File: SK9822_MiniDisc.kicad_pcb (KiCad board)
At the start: 4 copper layers, 220 x 220 mm, 341 parts, among them P1 CONN_01X04, P2 CONN_01X04

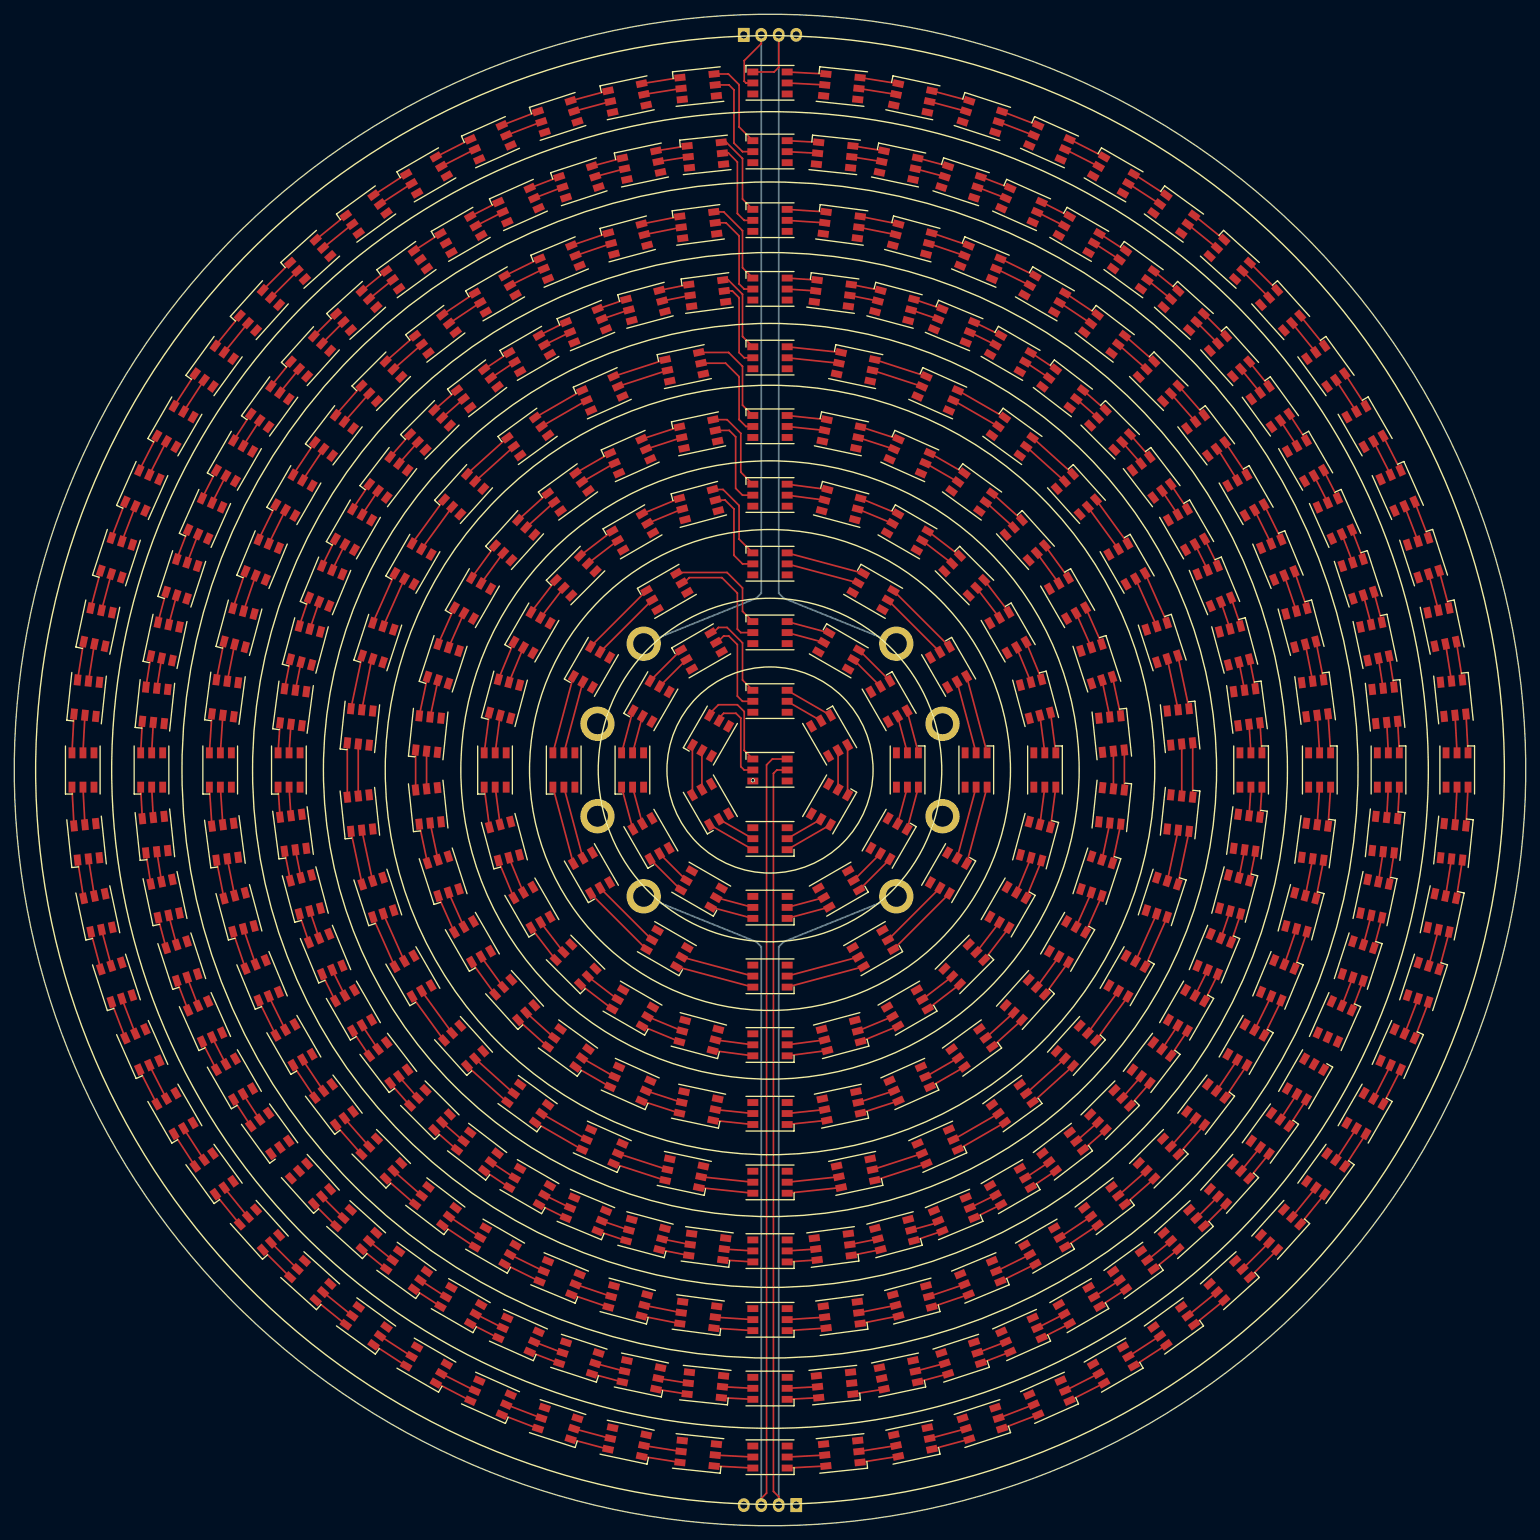
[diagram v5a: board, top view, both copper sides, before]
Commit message: Grounds laid
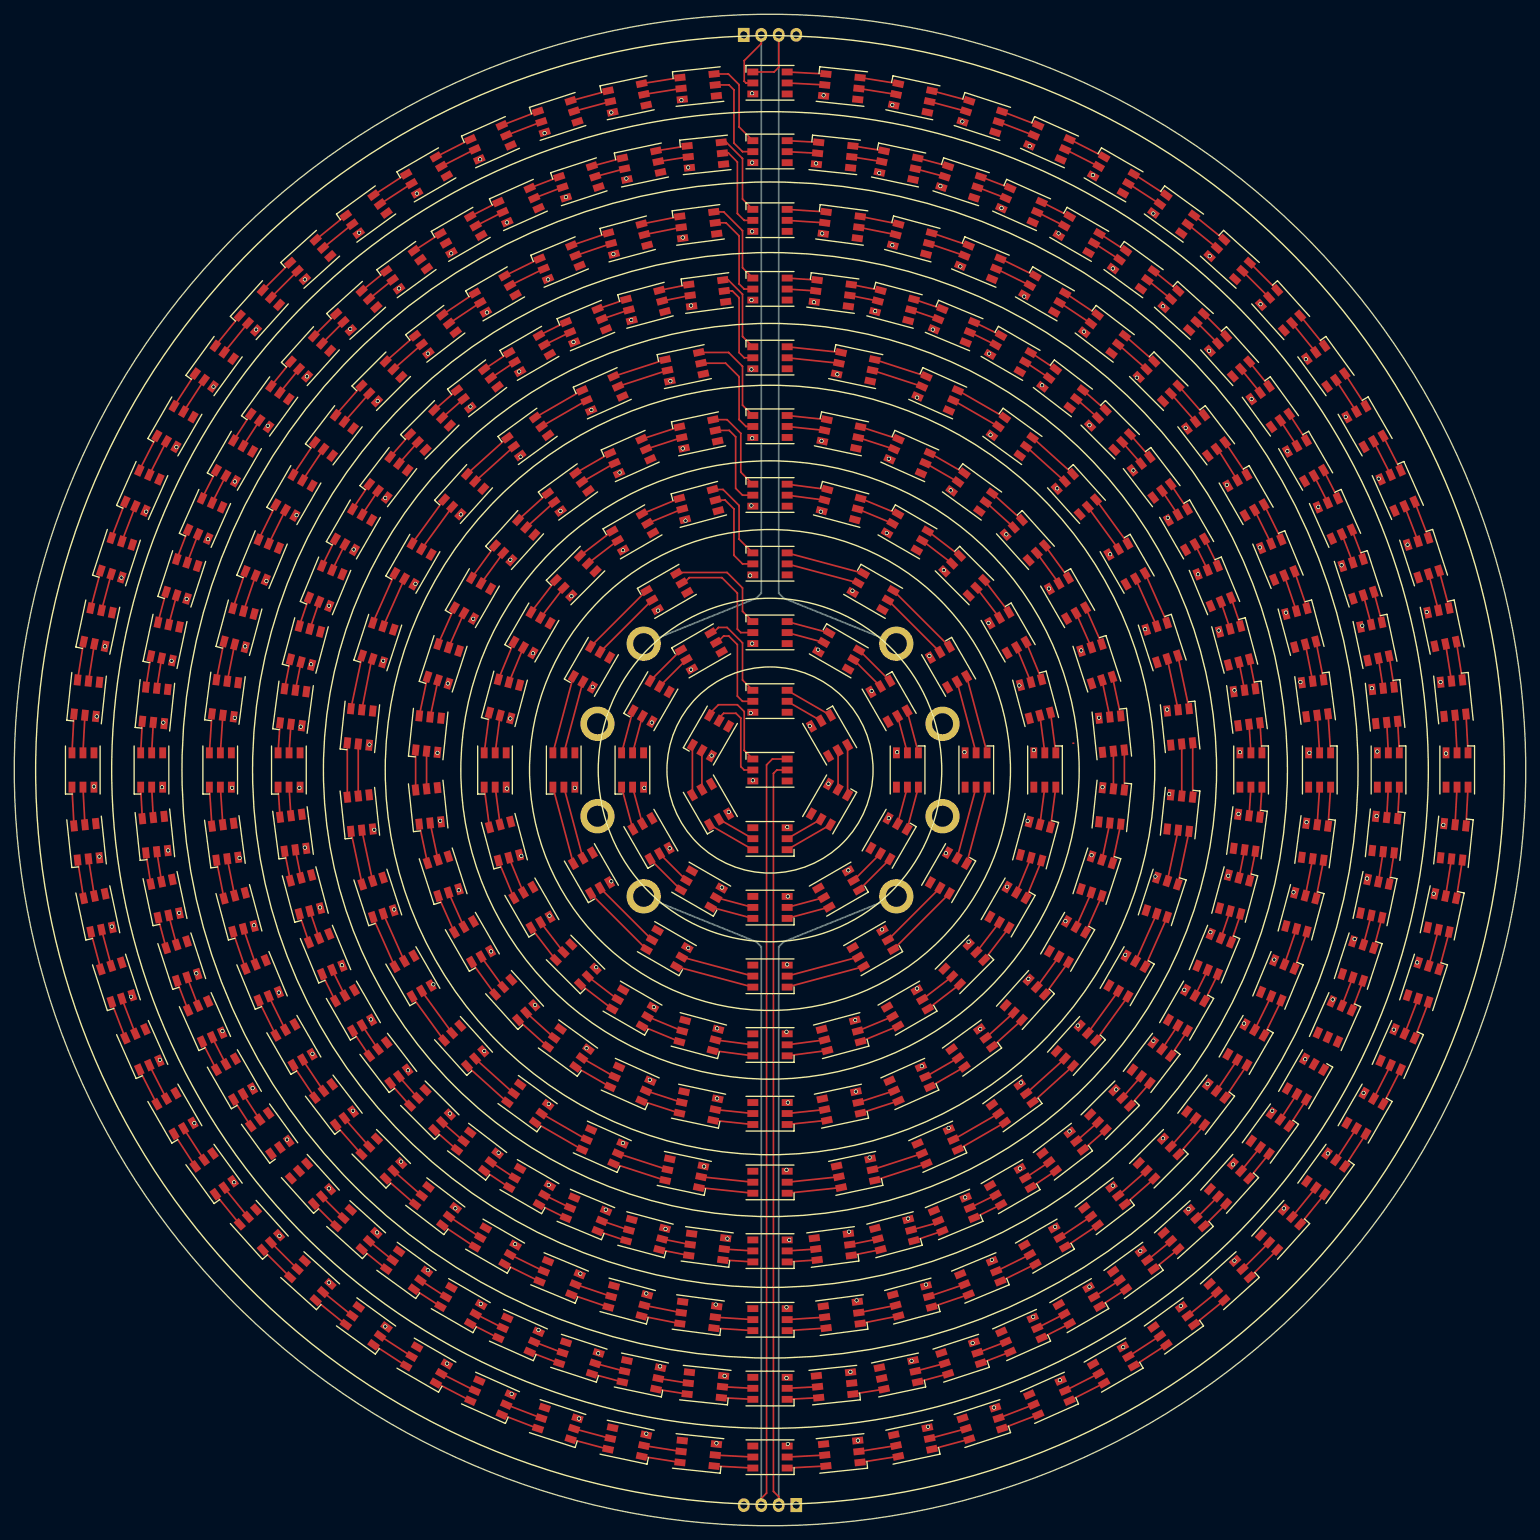
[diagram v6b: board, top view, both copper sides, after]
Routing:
- net GND: track 751.4 -> 4051.5 mm, vias 1 -> 329

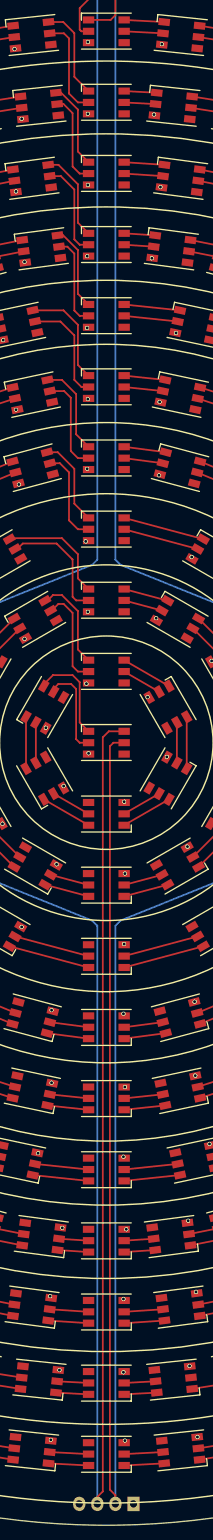
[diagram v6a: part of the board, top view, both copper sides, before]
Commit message: starting gnd plane
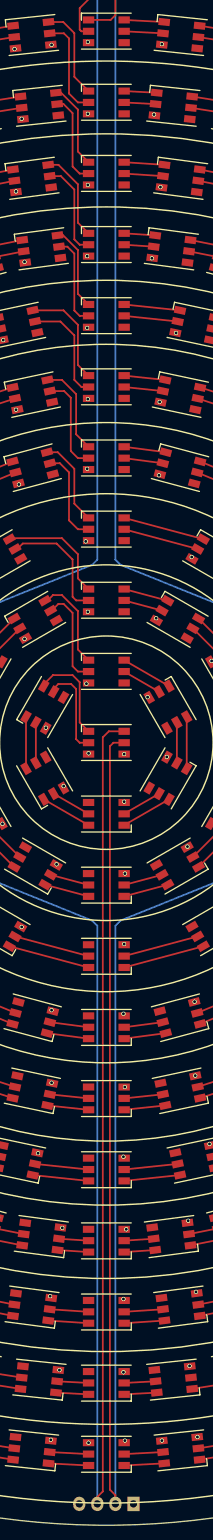
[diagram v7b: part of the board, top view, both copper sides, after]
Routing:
- net VCC: track 0.00 -> 2313.1 mm, vias 0 -> 5

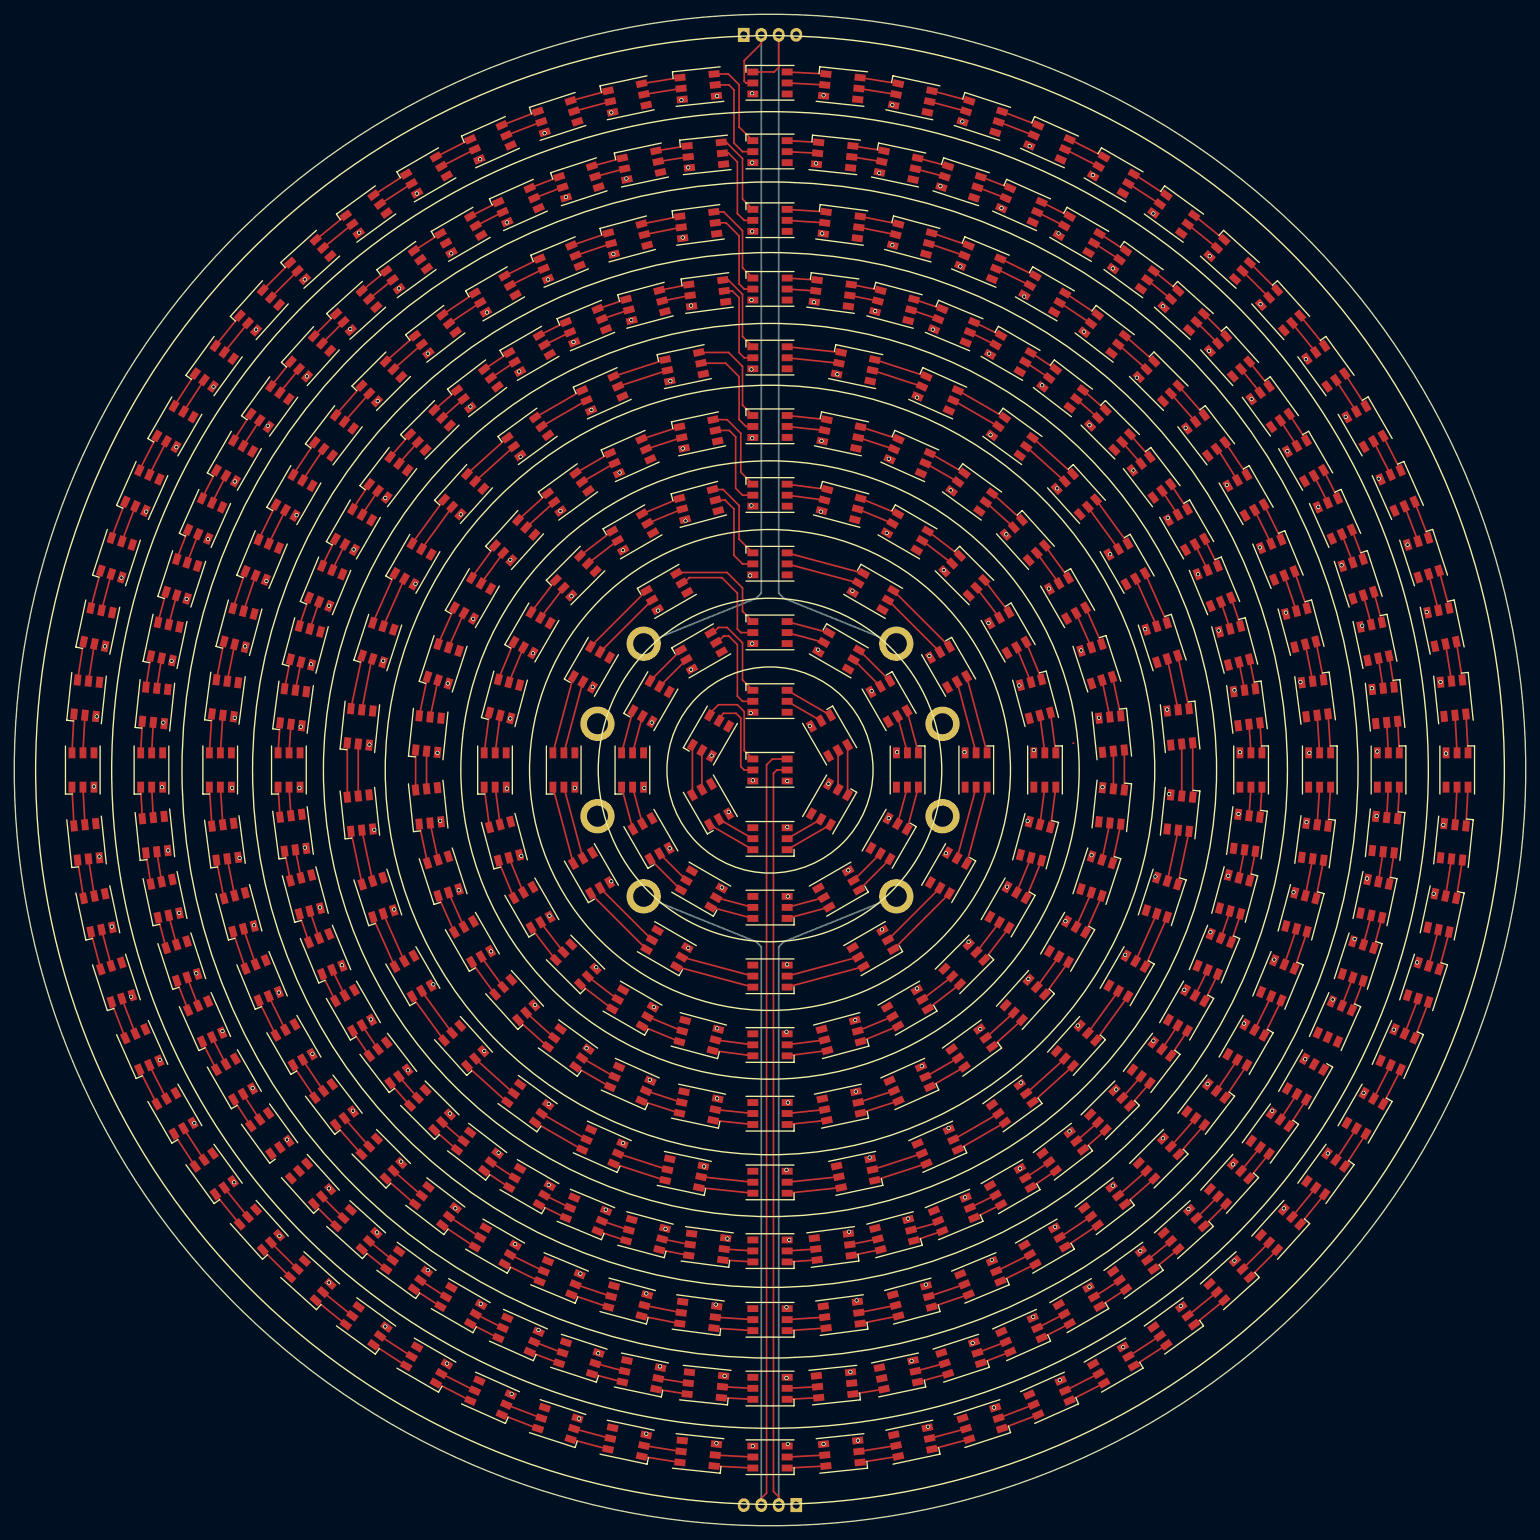
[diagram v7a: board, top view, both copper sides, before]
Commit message: more gnd plane
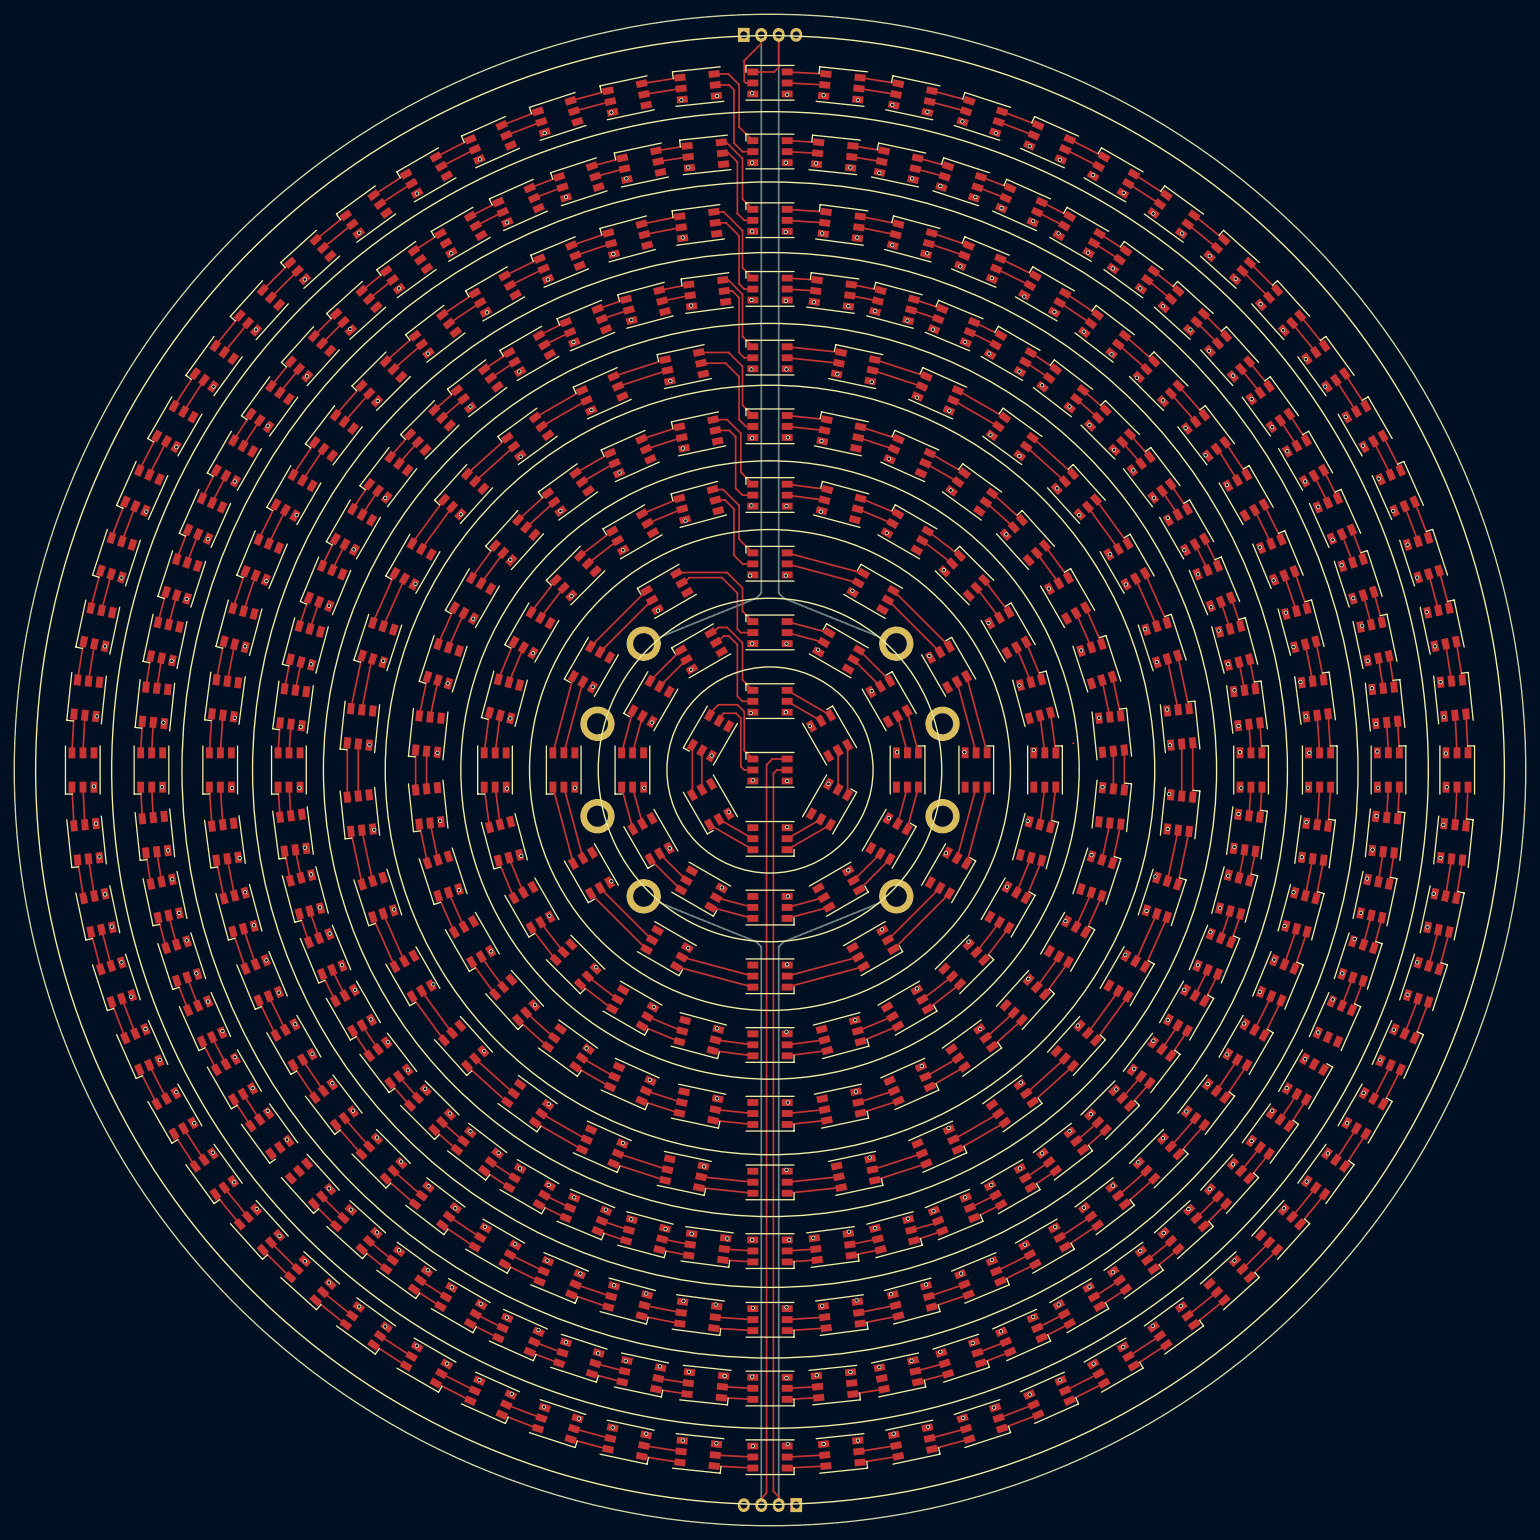
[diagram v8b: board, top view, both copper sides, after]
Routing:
- net VCC: track 2313.1 -> 3179.4 mm, vias 5 -> 173
